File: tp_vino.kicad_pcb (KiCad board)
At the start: 2 copper layers, 95 parts, among them J1 TB_1X2, J10 TB_1X2, J2 TB_1X2, J3 TB_1X2, J4 TB_1X2, J5 TB_1X2, J6 TB_1X2, J7 TB_1X2, J8 TB_1X2, J9 TB_1X2, P1 CONN_02X02, P10 CONN_01X02, P11 CONN_01X06, P12 CONN_01X06, P2 USB_OTG, P3 CONN_01X06, P4 CONN_01X06, P5 CONN_02X02, P6 CONN_01X02, P7 CONN_01X02, P8 CONN_01X02, P9 CONN_01X02, Q1 BC849, Q2 BC849, Q3 BC849, Q4 BC849, Q5 BC849, SW1 TEC_1, SW2 TEC_1, SW3 TEC_1, SW4 TEC_1, U1 ST3232E, U2 LM2576HVS-5, U3 NCP1117ST33T3G, U4 LM317_SOT223, U5 LM317_SOT223, U6 LM35-LP

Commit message: Algunas modificaciones en el circuito  oreno el pcb.
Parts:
- removed FB1, FB2: MMZ1608B601C, Diodes_SMD:SOD-123
- removed P3, P4: CONN_01X06, Pin_Headers:Pin_Header_Angled_1x06
- P10, P6, P7, P8, P9: footprint Pin_Headers:Pin_Header_Angled_1x02 -> Pin_Headers:Pin_Header_Straight_1x02
- P11, P12: footprint Pin_Headers:Pin_Header_Angled_1x06 -> Pin_Headers:Pin_Header_Straight_1x06
- P5: footprint Pin_Headers:Pin_Header_Angled_2x02 -> Pin_Headers:Pin_Header_Straight_2x02
- Q2, Q3, Q4, Q5: footprint TO_SOT_Packages_SMD:SOT-323 -> TO_SOT_Packages_SMD:SOT-23
- moved U4 178.8 mm to (67.3, 30.5)
- moved R5 166.2 mm to (67.3, 36.8)
- moved P6 163.7 mm to (45.7, 21.6), turned to 90 degrees
- moved Q1 140.8 mm to (124.5, 163.8)
- moved v_tension1 132.6 mm to (48.3, 44.5)
- moved P8 116.9 mm to (153.7, 132.1), turned to 90 degrees
- moved U6 97.4 mm to (141.0, 41.9)
- moved L1 95.5 mm to (41.9, 91.4), turned to 180 degrees
- moved RV3 79.1 mm to (141.0, 26.7)
- moved J9 65.4 mm to (189.2, 29.2)
- moved P9 65.4 mm to (204.5, 41.9)
- moved v_out_1 65.4 mm to (200.7, 29.2)
- moved J10 49.1 mm to (247.7, 29.2)
- moved P10 49.1 mm to (227.3, 41.9)
- moved v_out_2 49.1 mm to (223.5, 29.2)
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
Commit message: Modificaciones en el schematic debida a los warning por powerflag y conectores mal definido como input en vez de pasive.
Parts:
- turned C12 to 270 degrees
- turned Q2 to 270 degrees
- turned Q3 to 270 degrees
- turned Q4 to 270 degrees
- turned Q5 to 270 degrees
- turned U3 to 90 degrees
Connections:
- net /SIM800L/Rx_sim800 renamed /RS232_TTL/TTL_RS232_TXD1

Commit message: Modificaciones en el schematic dado los componentes comprados empiezo a ordenar los componentes en una dimension estimada de 10x6 cm.
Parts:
- added D12: D, Diodes_SMD:MELF_Handsoldering, F.Cu at (78.7, 174.0)
- added P3: CONN_01X03, Pin_Headers:Pin_Header_Straight_1x03, F.Cu at (59.7, 179.1)
- added P4: CONN_01X03, Pin_Headers:Pin_Header_Straight_1x03, F.Cu at (104.1, 153.7)
- added R27: R, SMD_Packages:SMD-1206_Pol, F.Cu at (59.7, 167.6)
- added U7: SIM800L, sim800L_ok:sim, F.Cu at (76.2, 170.2)
- C1, C10, C11, C12, C2, C3, C4, C5, C9: footprint Capacitors_SMD:C_0805 -> Capacitors_SMD:C_1206
- C6: footprint Capacitors_ThroughHole:C_Radial_D13_L21_P5 -> Capacitors_ThroughHole:C_Radial_D10_L25_P5
- C7: footprint Capacitors_ThroughHole:C_Radial_D10_L20_P5 -> Capacitors_ThroughHole:C_Radial_D10_L25_P5
- C8: footprint Capacitors_ThroughHole:C_Radial_D10_L25_P5 -> Capacitors_ThroughHole:C_Radial_D5_L6_P2.5
- D1, D2, D3, D7: footprint Diodes_SMD:SOD-123 -> Diodes_SMD:MELF_Handsoldering
- D10, D11, D4, D5, D8, D9: footprint LEDs:LED_1206 -> Diodes_SMD:MELF_Handsoldering
- D6: value ZENER_4,3V_1N4731 -> ZENER; footprint Diodes_SMD:SOD-123 -> Diodes_SMD:MELF_Handsoldering
- J1, J10, J2, J3, J4, J5, J6, J7, J8, J9: footprint Connect:bornier2 -> Connect:AK300-2
- P9: value CONN_01X02 -> CONN_01X03; footprint Pin_Headers:Pin_Header_Straight_1x02 -> Pin_Headers:Pin_Header_Straight_1x03
- U3: footprint TO_SOT_Packages_SMD:SOT-323 -> TO_SOT_Packages_SMD:TO-252-2Lead
- U4, U5: footprint TO_SOT_Packages_SMD:SOT-323 -> TO_SOT_Packages_THT:TO-220_Neutral123_Horizontal
- moved P6 130.7 mm to (92.7, 143.5), turned to 180 degrees
- moved J6 128.6 mm to (104.1, 142.2)
- moved U4 119.5 mm to (97.8, 146.1), turned to 90 degrees
- moved R5 117.1 mm to (92.7, 151.1), turned to 90 degrees
- moved v_tension1 104.2 mm to (87.6, 141.0), turned to 180 degrees
- moved D5 76.9 mm to (47.0, 141.0), turned to 180 degrees
- moved L1 66.1 mm to (43.2, 157.5), turned to 90 degrees
- moved U5 66.0 mm to (99.1, 156.2), turned to 90 degrees
- moved D2 64.8 mm to (52.1, 157.5)
- moved P2 63.9 mm to (69.8, 142.2), turned to 180 degrees
- moved D6 59.7 mm to (82.5, 174.0), turned to 90 degrees
- moved D3 59.7 mm to (68.6, 148.6), turned to 180 degrees
- moved D1 57.2 mm to (34.3, 167.6)
- moved C8 56.8 mm to (59.7, 161.3)
- moved P8 54.7 mm to (106.7, 160.0)
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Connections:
- net Net-(J6-Pad2) renamed /LM35_LM317_POTE/Vout
- net Net-(J8-Pad2) renamed /LM35_LM317_POTE/Iout
- D6 pad 1: Net-(D6-Pad1) -> GND
- D6 pad 2: GND -> Net-(D12-Pad1)
- D7 pad 2: Net-(D6-Pad1) -> Net-(D12-Pad2)
- P9 pad 1: Net-(J9-Pad1) -> +3.3V
- P9 pad 2: Net-(J9-Pad2) -> Net-(P9-Pad2)
- R2 pad 1: Net-(Q1-Pad1) -> Net-(R2-Pad1)
- R2 pad 2: Net-(R2-Pad2) -> Net-(Q1-Pad1)
- v_out_1 pad 1: Net-(J9-Pad1) -> Net-(P4-Pad2)
- v_out_1 pad 2: Net-(J9-Pad1) -> Net-(J9-Pad2)
- v_out_1 pad 3: Net-(J9-Pad2) -> Net-(J9-Pad1)
- v_out_2 pad 1: Net-(J10-Pad1) -> Net-(P9-Pad2)
- v_out_2 pad 2: Net-(J10-Pad1) -> Net-(J10-Pad2)
- v_out_2 pad 3: Net-(J10-Pad2) -> Net-(J10-Pad1)

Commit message: Modificaciones en el schematico.Cambio dimension a 10x7 cm.
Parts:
- U4, U5: footprint TO_SOT_Packages_THT:TO-220_Neutral123_Horizontal -> TO_SOT_Packages_THT:TO-220_Neutral123_Vertical
- v_current1, v_tension1: footprint Potentiometers:Potentiometer_Trimmer-Piher_PT15-V15_horizontal -> Potentiometers:Potentiometer_Bourns_3296W_3-8Zoll_Inline_ScrewUp
- moved C12 146.3 mm to (132.8, 69.6), turned to 0 degrees
- moved C11 139.4 mm to (139.2, 69.6), turned to 180 degrees
- moved SW4 139.3 mm to (132.8, 62.7), turned to 180 degrees
- moved R14 134.7 mm to (132.8, 66.8), turned to 180 degrees
- moved SW3 132.7 mm to (139.2, 62.7), turned to 180 degrees
- moved R10 131.9 mm to (132.6, 72.6), turned to 180 degrees
- moved C10 131.4 mm to (145.5, 69.6), turned to 0 degrees
- moved P6 128.8 mm to (204.2, 79.0), turned to 0 degrees
- moved R13 127.5 mm to (139.4, 66.8), turned to 0 degrees
- moved P4 127.1 mm to (203.5, 74.4), turned to 270 degrees
- moved J6 126.9 mm to (203.7, 63.5), turned to 270 degrees
- moved SW2 126.3 mm to (145.5, 62.7), turned to 180 degrees
- moved C9 124.3 mm to (152.7, 69.6), turned to 0 degrees
- moved R9 124.3 mm to (139.4, 72.6), turned to 0 degrees
- moved J10 122.1 mm to (174.5, 127.0), turned to 180 degrees
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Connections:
- P1 pad 1: /RS232_TTL/TTL_RS232_TXD1 -> /RS232_TTL/TTL_RS232_RXD1
- P1 pad 3: /RS232_TTL/TTL_RS232_RXD1 -> /RS232_TTL/TTL_RS232_TXD1
- R15 pad 1: Net-(P12-Pad5) -> Net-(P12-Pad3)
- R16 pad 1: Net-(P12-Pad5) -> Net-(P12-Pad3)
- R18 pad 1: Net-(P12-Pad3) -> Net-(P12-Pad5)
- R19 pad 1: Net-(P12-Pad3) -> Net-(P12-Pad5)
- U1 pad 11: Net-(J1-Pad1) -> Net-(J1-Pad2)
- U1 pad 12: Net-(J1-Pad2) -> Net-(J1-Pad1)
- U1 pad 13: Net-(J4-Pad1) -> Net-(J4-Pad2)
- U1 pad 14: Net-(J4-Pad2) -> Net-(J4-Pad1)
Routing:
- net GND: track 0.00 -> 96.8 mm
- net +5V: track 0.00 -> 65.1 mm
- net Net-(D2-Pad2): track 0.00 -> 27.2 mm
- net Net-(J1-Pad1): track 0.00 -> 27.0 mm
- net Net-(J3-Pad1): track 0.00 -> 26.8 mm
- net Net-(J1-Pad2): track 0.00 -> 23.3 mm
- net Net-(J4-Pad2): track 0.00 -> 22.3 mm
- net Net-(J3-Pad2): track 0.00 -> 21.6 mm
- net Net-(J4-Pad1): track 0.00 -> 18.4 mm
- net Net-(J2-Pad2): track 0.00 -> 16.6 mm
- net Net-(J2-Pad1): track 0.00 -> 14.8 mm
- net Net-(C12-Pad1): track 0.00 -> 9.93 mm
- net Net-(R5-Pad1): track 0.00 -> 8.26 mm
- net Net-(Q1-Pad1): track 0.00 -> 6.46 mm
- net Net-(C4-Pad1): track 0.00 -> 5.63 mm
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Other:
- net class Default: trace_width 0.25 -> 1
- rule trace_min: 0.2 -> 1

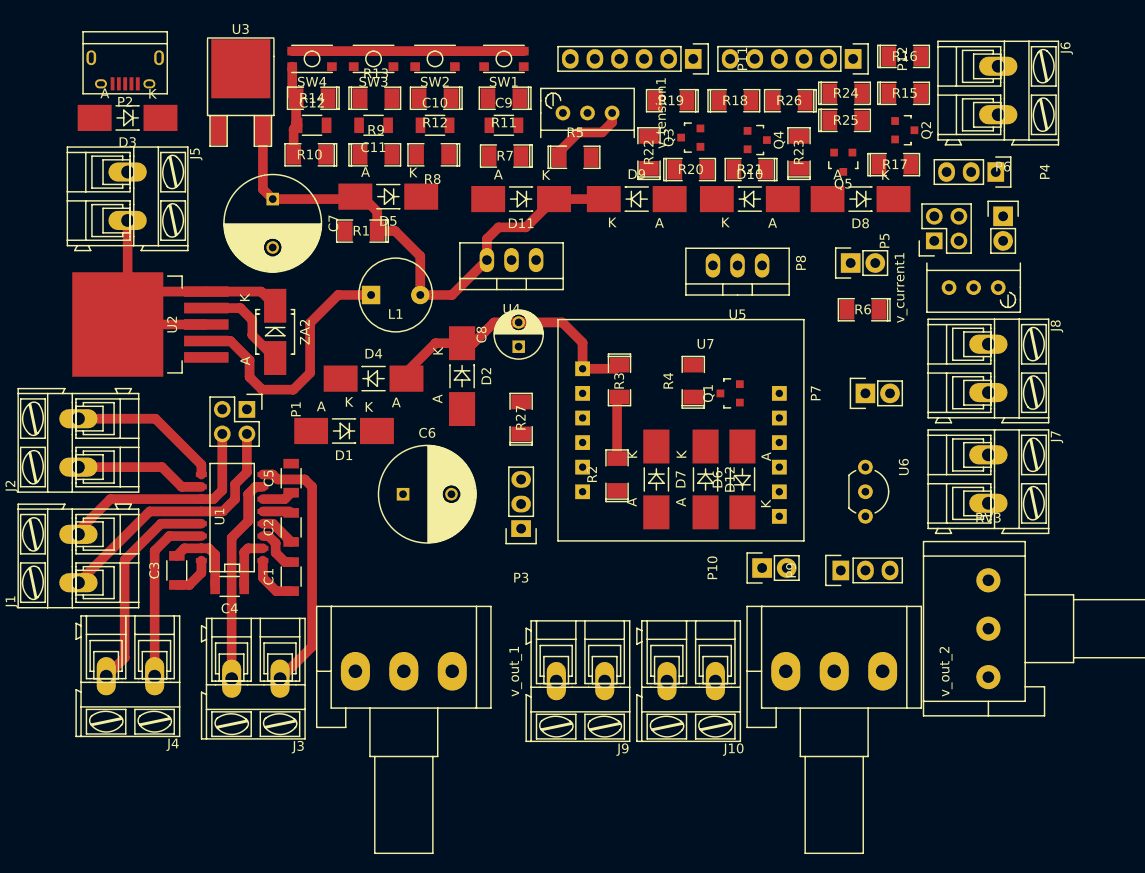
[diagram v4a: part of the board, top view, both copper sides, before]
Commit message: Ruteo del PCB, agrego una salida de 5v y 3v en el esquematico
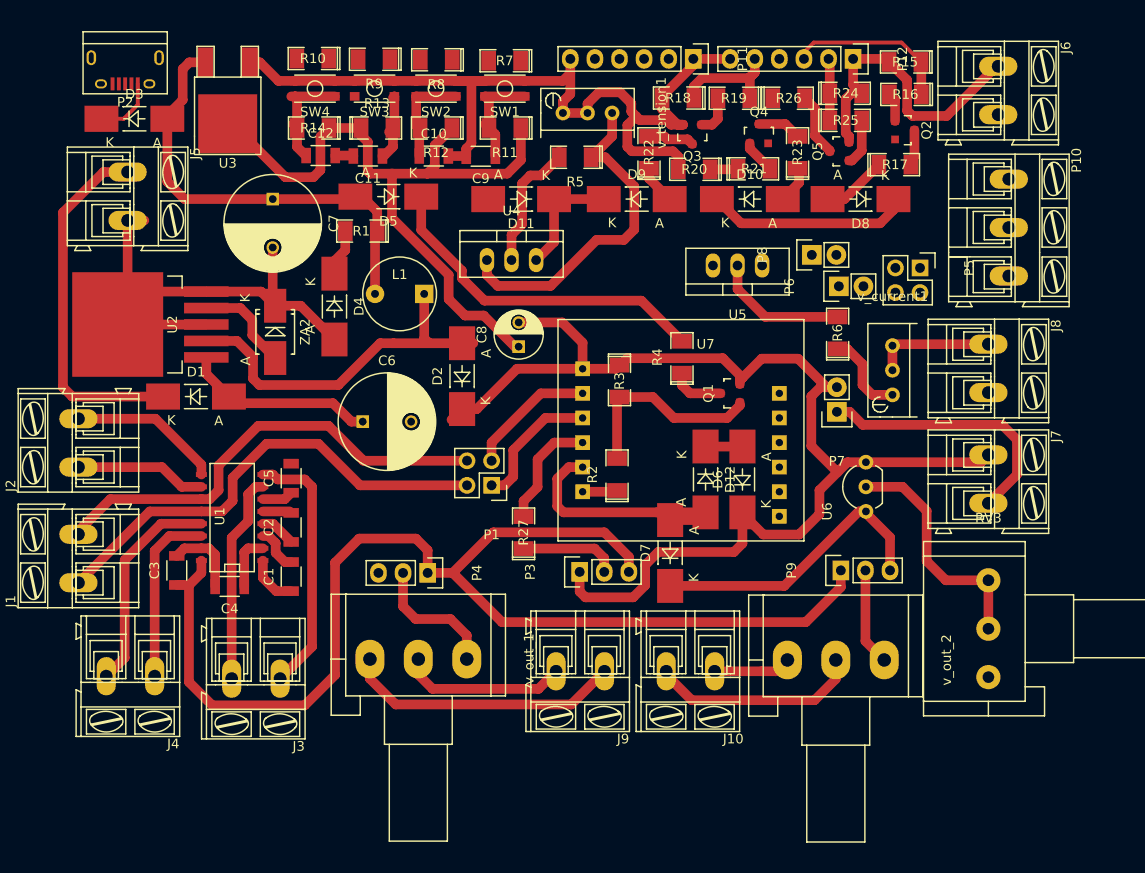
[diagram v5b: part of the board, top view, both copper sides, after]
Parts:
- J10: value TB_1X2 -> PotO.Out
- J6: value TB_1X2 -> V.RegOut
- J7: value TB_1X2 -> Temp.Out
- J8: value TB_1X2 -> C.RegOut
- J9: value TB_1X2 -> PotTOut
- P10: value CONN_01X02 -> CONN_01X03; footprint Pin_Headers:Pin_Header_Straight_1x02 -> Connect:AK300-3
- P4: value CONN_01X03 -> Pot2_Out
- P5: value CONN_02X02 -> C.reg.in
- P6: value CONN_01X02 -> V_regOut
- P7: value CONN_01X02 -> Temp_Out
- P8: value CONN_01X02 -> C_RegOut
- P9: value CONN_01X03 -> PotO_Out
- moved P4 71.8 mm to (144.8, 115.8)
- moved P10 47.6 mm to (204.8, 75.2), turned to 270 degrees
- moved P1 26.5 mm to (151.4, 106.8), turned to 180 degrees
- moved P6 18.4 mm to (187.2, 86.2), turned to 90 degrees
- moved D1 15.7 mm to (120.9, 97.6), turned to 0 degrees
- moved v_current1 15.6 mm to (192.8, 97.4), turned to 0 degrees
- moved R27 11.8 mm to (154.7, 111.7)
- moved R10 9.95 mm to (132.9, 62.7)
- moved R9 9.87 mm to (139.2, 62.8), turned to 180 degrees
- moved R7 9.84 mm to (152.7, 62.9)
- moved R8 9.82 mm to (145.7, 62.8)
- moved C6 8.57 mm to (138.1, 100.2)
- moved D4 8.47 mm to (135.2, 88.3), turned to 270 degrees
- moved D7 7.73 mm to (169.8, 113.8), turned to 90 degrees
- moved P3 7.52 mm to (160.5, 115.7), turned to 90 degrees
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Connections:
- J8 pad 1: GND -> /LM35_LM317_POTE/Iout
- J8 pad 2: /LM35_LM317_POTE/Iout -> GND
- P10 pad 1: Net-(J10-Pad1) -> +5V
- P10 pad 2: Net-(J10-Pad2) -> GND
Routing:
- net GND: track 96.8 -> 311.3 mm
- net +3.3V: track 4.33 -> 202.5 mm
- net +5V: track 65.1 -> 120.6 mm
- net Net-(D1-Pad1): track 0.00 -> 37.2 mm
- net Net-(D5-Pad1): track 0.00 -> 35.6 mm
- net Net-(J9-Pad1): track 0.00 -> 28.8 mm
- net Net-(J7-Pad2): track 0.00 -> 28.1 mm
- net Net-(R5-Pad1): track 8.26 -> 35.3 mm
- net Net-(D12-Pad2): track 0.00 -> 25.5 mm
- net Net-(J1-Pad2): track 23.3 -> 48.5 mm
- net Net-(RV3-Pad1): track 0.00 -> 24.7 mm
- net Net-(J1-Pad1): track 27.0 -> 49.3 mm
- net Net-(J10-Pad2): track 0.00 -> 21.8 mm
- net Net-(C6-Pad1): track 0.00 -> 19.9 mm
- net Net-(P12-Pad3): track 0.00 -> 17.4 mm
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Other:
- net class aprox_pad added: clearance 0.2, trace_width 0.6, via_dia 0.6, via_drill 0.4
- rule trace_min: 1 -> 0.4

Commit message: Ruteo del PCB top first end. Falta button layer
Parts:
- P10: value CONN_01X03 -> 3.3_GND_5V
- moved P5 27.3 mm to (168.3, 83.0), turned to 0 degrees
- moved P8 6.92 mm to (191.4, 82.9)
- moved J5 6.64 mm to (110.6, 80.2), turned to 90 degrees
- moved P6 4.21 mm to (191.5, 86.5)
- moved P3 4.01 mm to (164.5, 115.4), turned to 270 degrees
- moved U5 3.89 mm to (180.7, 84.0)
- moved R16 2.36 mm to (195.2, 64.3), turned to 270 degrees
- moved C8 2.20 mm to (152.6, 90.9), turned to 0 degrees
- moved R15 2.13 mm to (192.4, 64.4), turned to 270 degrees
- moved P10 1.73 mm to (203.1, 75.1)
- moved R17 0.67 mm to (193.7, 73.8)
- moved J6 0.41 mm to (203.3, 63.6)
- moved Q2 0.39 mm to (194.0, 70.5)
- turned D8 to 0 degrees
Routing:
- net GND: track 311.3 -> 396.4 mm
- net /LM35_LM317_POTE/Vout: track 14.6 -> 48.5 mm
- net +5V: track 120.6 -> 145.6 mm
- net Net-(J7-Pad2): track 28.1 -> 48.3 mm
- net /LM35_LM317_POTE/Iout: track 12.5 -> 31.5 mm
- net +3.3V: track 202.5 -> 183.7 mm
- net Net-(P12-Pad4): track 2.89 -> 19.5 mm
- net Net-(P5-Pad2): track 0.00 -> 10.2 mm
- net Net-(D1-Pad1): track 37.2 -> 28.1 mm
- net Net-(R6-Pad2): track 14.0 -> 9.93 mm
- net Net-(D8-Pad2): track 6.78 -> 3.73 mm
- net Net-(Q2-Pad1): track 2.99 -> 4.90 mm
- net Net-(P3-Pad2): track 10.2 -> 8.82 mm

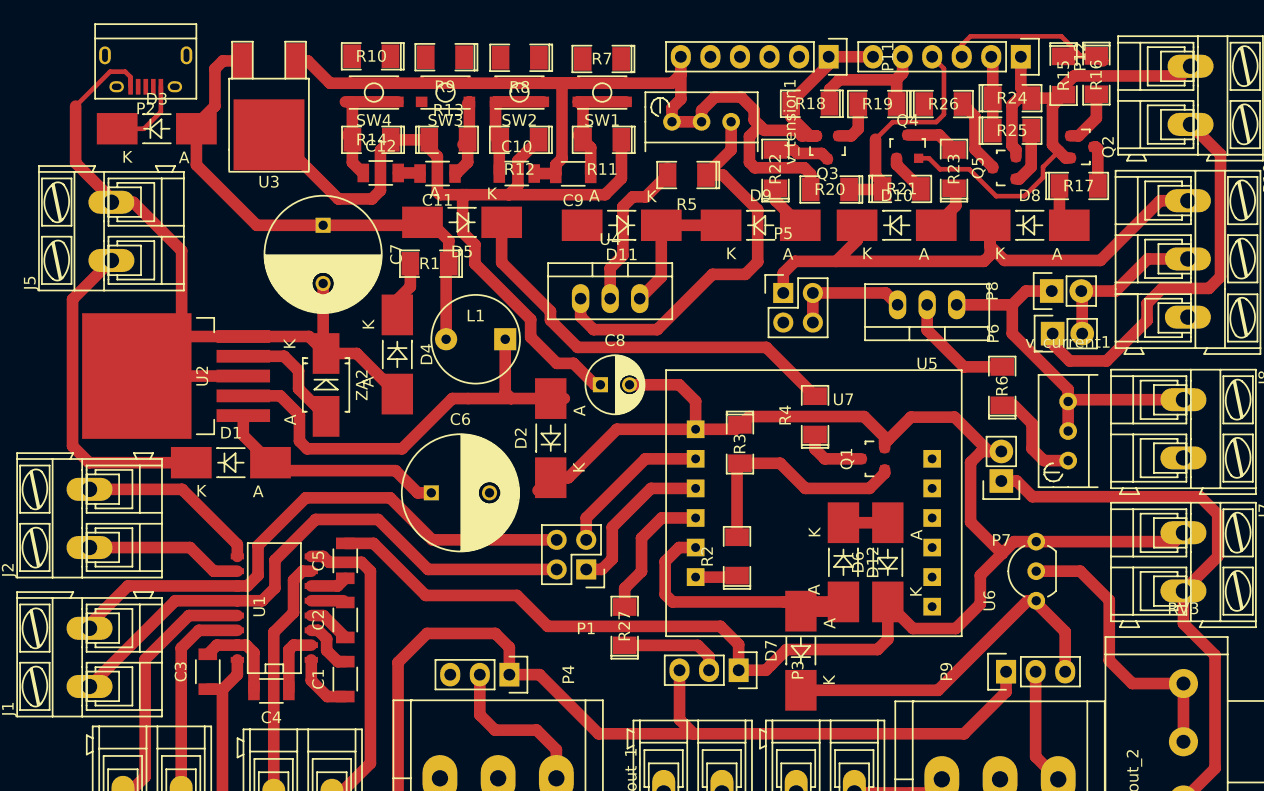
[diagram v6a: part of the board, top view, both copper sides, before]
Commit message: Ruteo del PCB top and button end. First Version
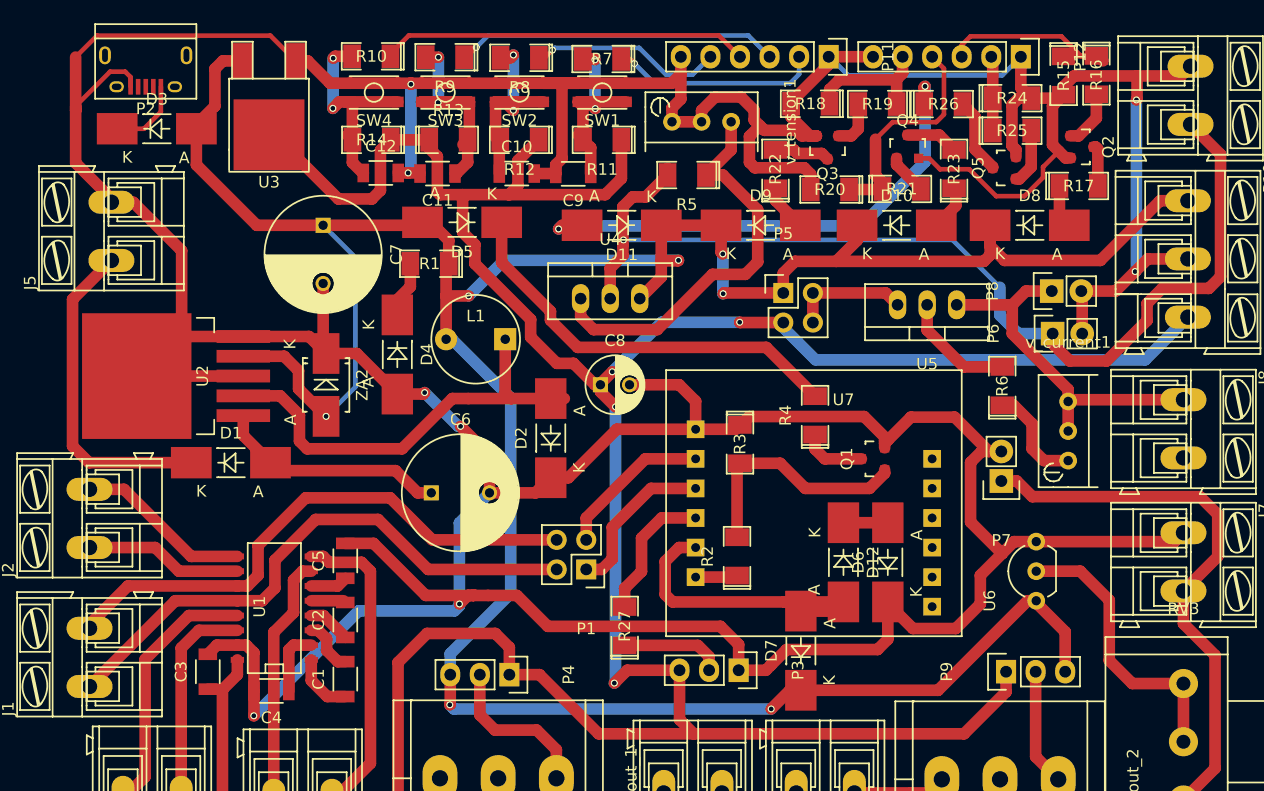
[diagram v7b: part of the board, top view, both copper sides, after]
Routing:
- net GND: track 396.4 -> 519.6 mm, vias 0 -> 9
- net +5V: track 145.6 -> 265.3 mm, vias 0 -> 7
- net +3.3V: track 183.7 -> 271.8 mm, vias 0 -> 4
- net Net-(D11-Pad2): track 0.00 -> 44.1 mm, vias 0 -> 2
- net /LM35_LM317_POTE/Vout: track 48.5 -> 90.6 mm, vias 0 -> 1
- net Net-(P11-Pad4): track 0.00 -> 31.6 mm
- net Net-(P11-Pad3): track 0.00 -> 27.8 mm, vias 0 -> 1
- net Net-(P11-Pad2): track 0.00 -> 18.0 mm, vias 0 -> 1
- net Net-(P11-Pad5): track 0.00 -> 16.7 mm, vias 0 -> 1
- net Net-(C11-Pad1): track 7.52 -> 20.3 mm, vias 0 -> 2
- net Net-(C10-Pad1): track 11.2 -> 19.0 mm, vias 0 -> 2
- net Net-(C12-Pad1): track 12.7 -> 20.4 mm, vias 0 -> 2
- net Net-(C9-Pad1): track 11.3 -> 18.3 mm, vias 0 -> 2
- net Net-(J2-Pad2): track 16.6 -> 16.0 mm
